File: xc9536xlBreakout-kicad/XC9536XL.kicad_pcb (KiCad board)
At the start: 2 copper layers, 29 parts, among them J1 19-36, J2 Conn_01x01, J3 JTAG, J4 Conn_01x03, J5 Conn_01x06, SW1 SW_DIP_x04, U1 XC9536XL-VQ44, U2 MIC5504-3.3YM5

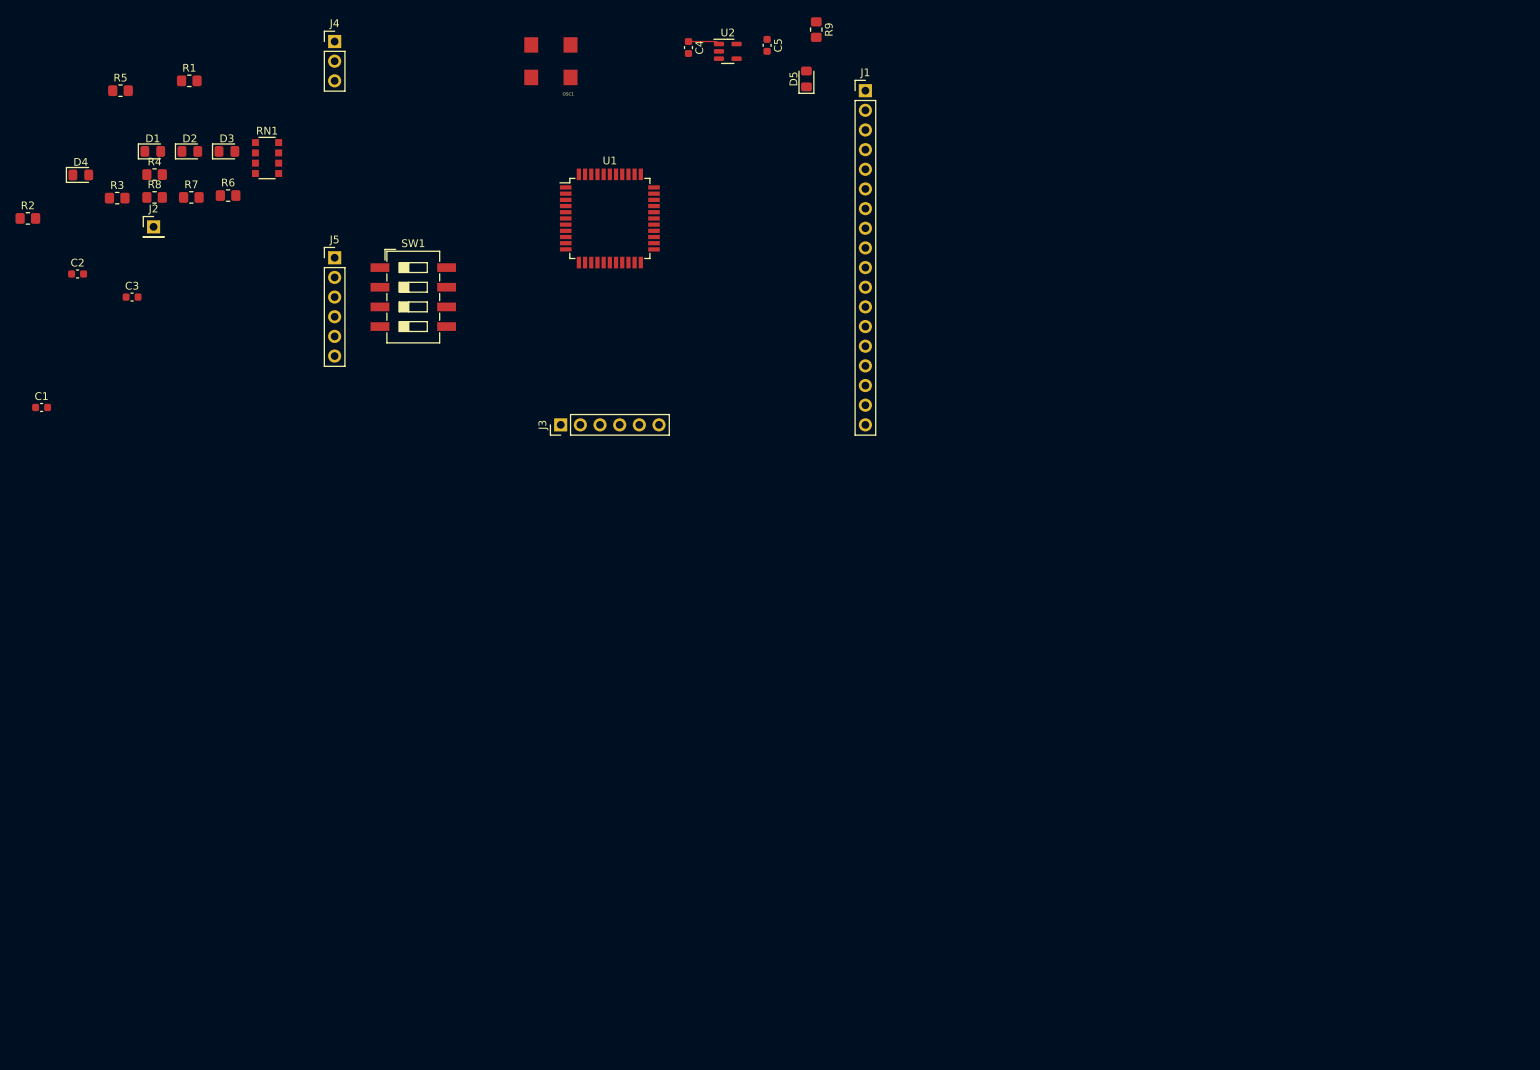
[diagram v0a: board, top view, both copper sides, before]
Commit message: Add files via upload
6.9.21 After Design Review
Notes
Check forward current/ voltage on LEDs
reassign led resistor values to be lower
throw in some other sized caps for vcc
make caps as close as possible to each power pin
osc should be on power side as close as possible to to uC
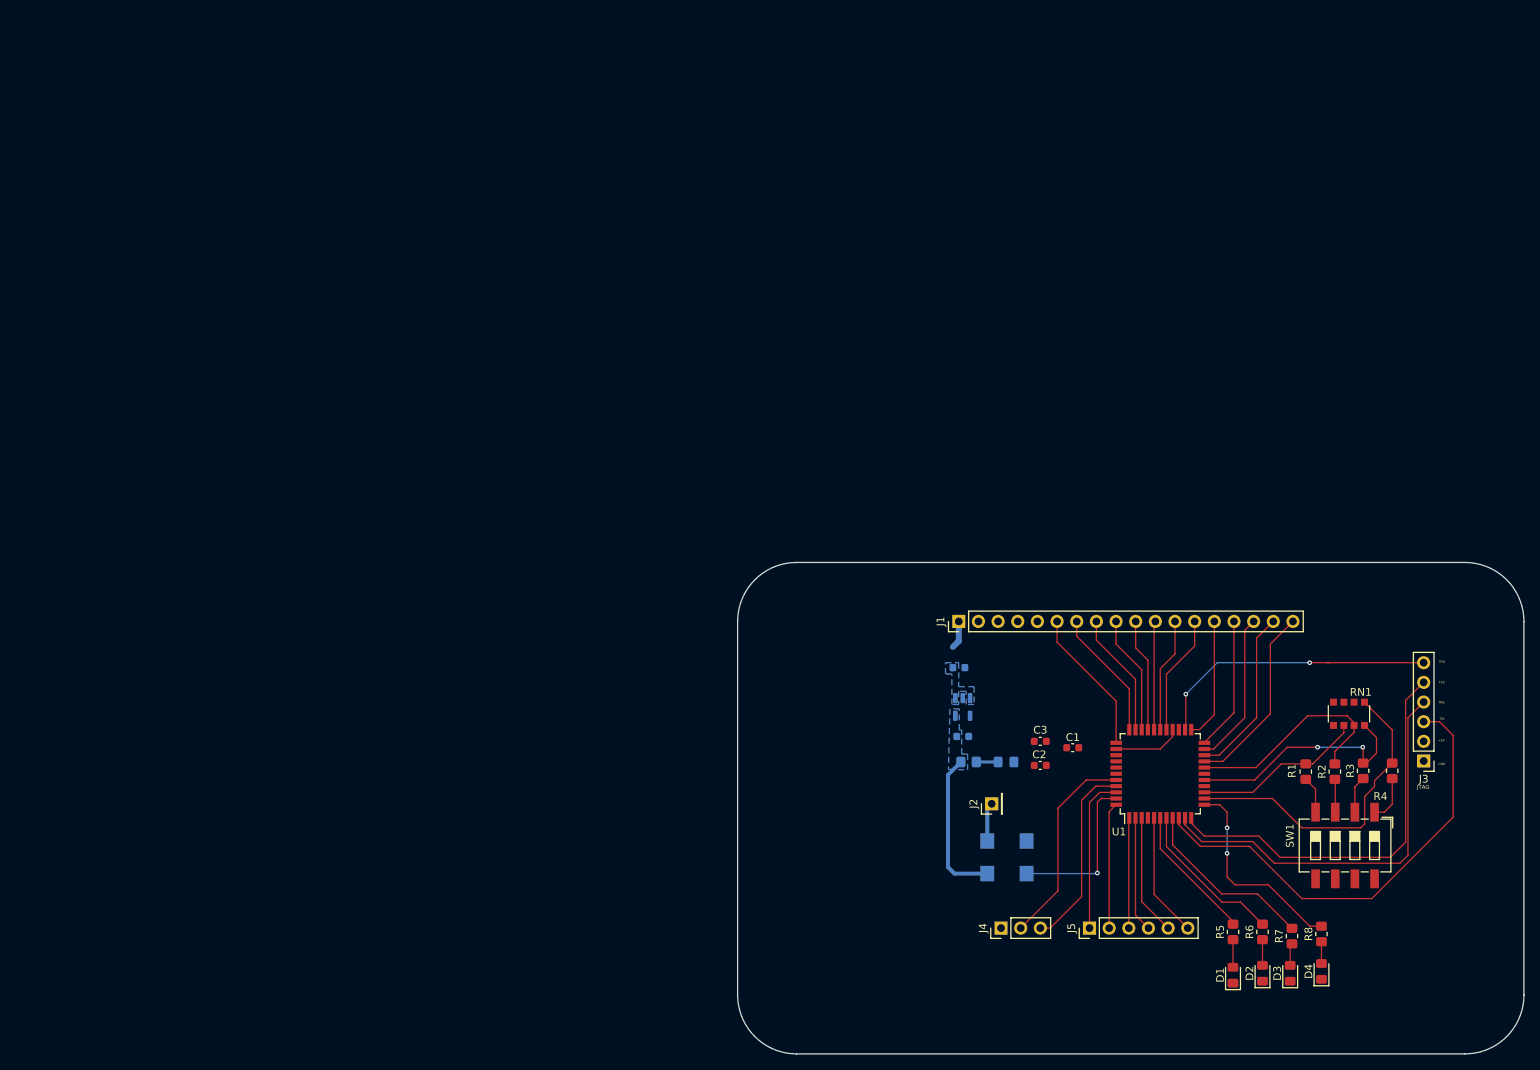
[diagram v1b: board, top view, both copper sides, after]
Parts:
- C4, C5, D5, OSC1, R9, U2: moved to B.Cu
- moved D4 190.5 mm to (202.4, 144.3), turned to 90 degrees
- moved R2 183.4 mm to (204.2, 118.5), turned to 90 degrees
- moved R5 180.2 mm to (191.0, 139.2), turned to 90 degrees
- moved R8 178.3 mm to (202.4, 139.4), turned to 90 degrees
- moved R4 177.5 mm to (211.6, 118.4), turned to 90 degrees
- moved R3 177.2 mm to (207.8, 118.4), turned to 90 degrees
- moved D1 175.5 mm to (191.0, 144.8), turned to 90 degrees
- moved D2 174.6 mm to (194.8, 144.5), turned to 90 degrees
- moved D3 173.6 mm to (198.4, 144.5), turned to 90 degrees
- moved R7 171.3 mm to (198.6, 139.7), turned to 90 degrees
- moved R1 169.6 mm to (200.4, 118.5), turned to 90 degrees
- moved R6 164.1 mm to (194.8, 139.2), turned to 90 degrees
- moved RN1 157.2 mm to (206.0, 111.0), turned to 90 degrees
- moved J4 143.3 mm to (161.0, 138.7), turned to 90 degrees
- moved C1 140.3 mm to (170.3, 115.4), turned to 180 degrees
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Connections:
- J5 pad 3: /P1-6 -> /P1-7
- J5 pad 4: /P1-7 -> /P1-6
- U1 pad 36: /P2-3 -> /P2-4
- U1 pad 37: /P2-4 -> /P2-3
- U2 pad 4: Net-(U2-Pad4) -> (no net)
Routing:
- net /TDI: track 0.00 -> 59.8 mm
- net /TMS: track 0.00 -> 52.8 mm
- net /TCK: track 0.00 -> 52.6 mm
- net /P1-15: track 0.00 -> 41.2 mm
- net /TDO: track 0.00 -> 37.3 mm, vias 0 -> 2
- net /P1-16: track 0.00 -> 30.8 mm, vias 0 -> 2
- net +3V3: track 0.00 -> 28.8 mm
- net /P1-17: track 0.00 -> 28.8 mm
- net /P1-13: track 0.00 -> 26.5 mm, vias 0 -> 2
- net /P1-1: track 0.00 -> 26.5 mm
- net /P1-2: track 0.00 -> 24.7 mm
- net /P2-17: track 0.00 -> 24.2 mm
- net /P1-12: track 0.00 -> 23.4 mm
- net /P1-14: track 0.00 -> 22.2 mm
- net /P2-16: track 0.00 -> 22.1 mm
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- added copper zone on B.Cu, net +3V3
- added copper zone on B.Cu, net +5V
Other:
- board outline added: 101.6 x 63.5 mm
- net class +3V3 added: clearance 0.1492, trace_width 0.5302, via_dia 1.054, via_drill 0.781
- net class POWER removed
- board text added: "+5V"
- board text added: "GND"
- board text added: "JTAG"
- board text added: "On LED"
- board text added: "TCK"
- board text added: "TDI"
- board text added: "TDO"
- board text added: "TMS"
